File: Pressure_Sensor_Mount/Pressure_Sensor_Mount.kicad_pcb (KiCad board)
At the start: 2 copper layers, 11.5 x 8.1 mm, 2 parts, among them J1 Conn_01x04_Pin

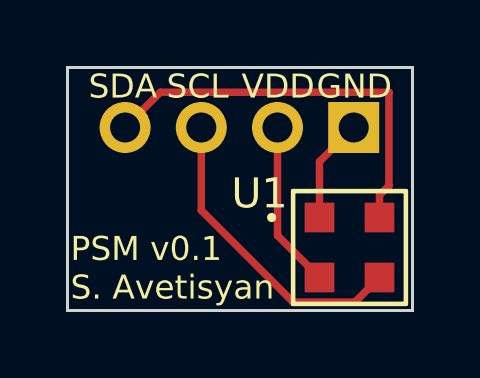
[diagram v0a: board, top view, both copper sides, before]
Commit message: Manufacturing Changes
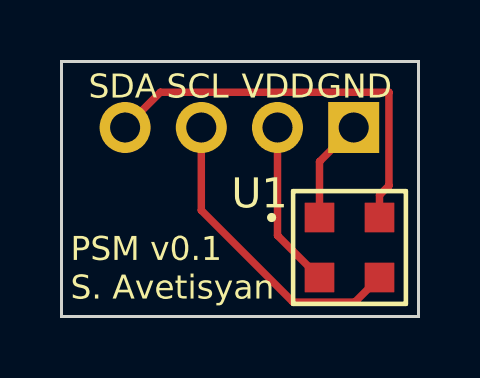
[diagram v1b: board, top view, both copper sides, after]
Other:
- board size 11.5 x 8.1 mm -> 11.9 x 8.5 mm
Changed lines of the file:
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@@
       (plot_on_all_layers_selection 0x0000000_00000000)
       (disableapertmacros false)
-      (usegerberextensions false)
-      (usegerberattributes true)
-      (usegerberadvancedattributes true)
-      (creategerberjobfile true)
+      (usegerberextensions true)
+      (usegerberattributes false)
+      (usegerberadvancedattributes false)
+      (creategerberjobfile false)
       (dashed_line_dash_ratio 12.000000)
       (dashed_line_gap_ratio 3.000000)
@@
       (psa4output false)
       (plotreference true)
-      (plotvalue true)
+      (plotvalue false)
       (plotinvisibletext false)
       (sketchpadsonfab false)
-      (subtractmaskfromsilk false)
+      (subtractmaskfromsilk true)
       (outputformat 1)
       (mirror false)
-      (drillshape 1)
+      (drillshape 0)
       (scaleselection 1)
-      (outputdirectory "")
+      (outputdirectory "./plots/")
     )
   )
@@
     )
   )
-  (gr_rect (start 138.6 86) (end 150.1 94.1)
+  (gr_rect (start 138.4 85.8) (end 150.3 94.3)
     (stroke (width 0.1) (type default)) (fill none) (layer "Edge.Cuts"))
   (gr_text "GND" (at 149.4 90.5) (layer "B.SilkS")
